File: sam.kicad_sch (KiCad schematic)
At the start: 45 parts, among them IC1 4164, IC15 MC6883, IC16 74LS244N, IC2 4164, IC3 4164, IC31 74LS02N, IC33 74LS138N, IC36 74LS132, IC37 GAL, IC4 4164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

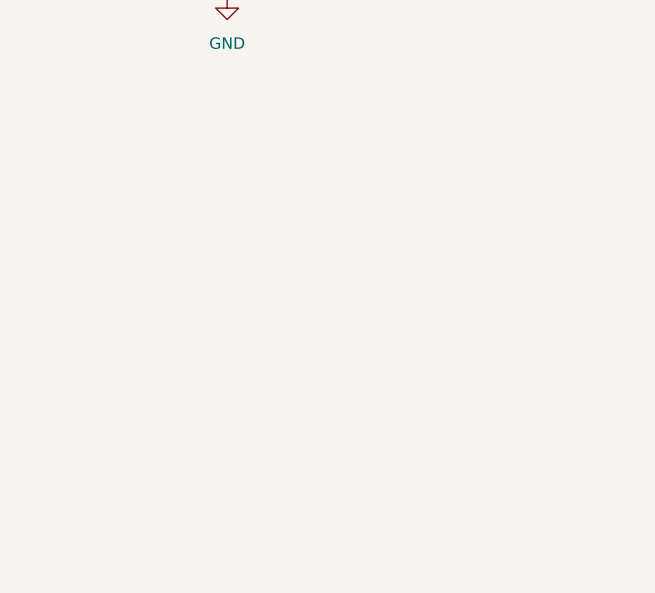
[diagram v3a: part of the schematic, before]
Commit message: add control for pia 3
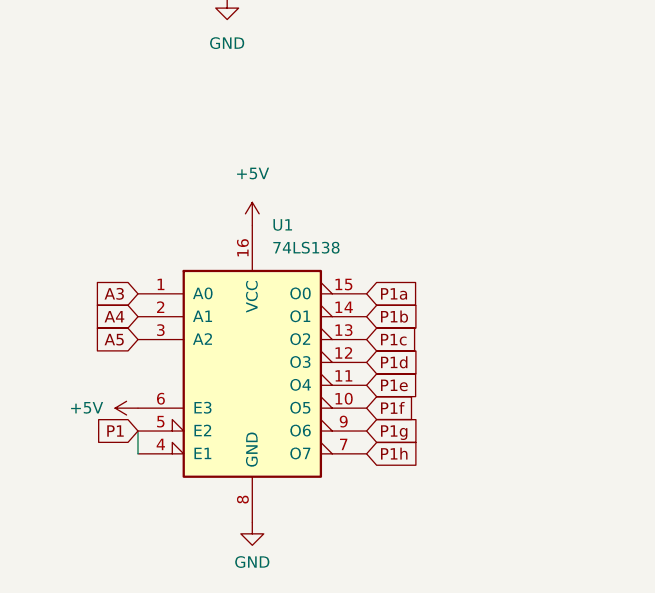
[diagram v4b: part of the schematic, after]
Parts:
- added U1: 74LS138, Package_DIP:DIP-16_W7.62mm, symbol 74xx:74LS138
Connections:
- net +5V: now also U1.16 (VCC), U1.6 (E3)
- net A3: now also U1.1 (A0)
- net A4: now also U1.2 (A1)
- net A5: now also U1.3 (A2)
- net GND: now also U1.8 (GND)
- net P1: now also U1.4 (E1), U1.5 (E2)
- new net P1a: U1.15 (O0)
- new net P1b: U1.14 (O1)
- new net P1c: U1.13 (O2)
- new net P1d: U1.12 (O3)
- new net P1e: U1.11 (O4)
- new net P1f: U1.10 (O5)
- new net P1g: U1.9 (O6)
- new net P1h: U1.7 (O7)
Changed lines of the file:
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@@
     (stroke (width 0) (type default))
   )
+  (wire (pts (xy 25.4 237.49) (xy 25.4 240.03))
+    (stroke (width 0) (type default))
+  )
   (wire (pts (xy 89.789 178.816) (xy 89.789 163.576))
     (stroke (width 0) (type default))
@@
     (stroke (width 0) (type default))
   )
+  (global_label "A5" (shape input) (at 25.4 227.33 180) (fields_autoplaced)
+    (effects (font (size 1.27 1.27)) (justify right))
+    (property "Intersheetrefs" "${INTERSHEET_REFS}" (at 20.7709 227.33 0)
+      (effects (font (size 1.27 1.27)) (justify right) hide)
+    )
+  )
   (global_label "DO0" (shape output) (at 22.606 171.45 180) (fields_autoplaced)
     (effects (font (size 1.27 1.27)) (justify right))
@@
     )
   )
+  (global_label "A3" (shape input) (at 25.4 222.25 180) (fields_autoplaced)
+    (effects (font (size 1.27 1.27)) (justify right))
+    (property "Intersheetrefs" "${INTERSHEET_REFS}" (at 20.7709 222.25 0)
+      (effects (font (size 1.27 1.27)) (justify right) hide)
+    )
+  )
   (global_label "~{WE}" (shape output) (at 110.617 112.141 180) (fields_autoplaced)
     (effects (font (size 1.27 1.27)) (justify right))
@@
     )
   )
+  (global_label "P1a" (shape input) (at 50.8 222.25 0) (fields_autoplaced)
+    (effects (font (size 1.27 1.27)) (justify left))
+    (property "Intersheetrefs" "${INTERSHEET_REFS}" (at 56.7595 222.25 0)
+      (effects (font (size 1.27 1.27)) (justify left) hide)
+    )
+  )
   (global_label "Z8" (shape output) (at 264.922 169.672 0) (fields_autoplaced)
     (effects (font (size 1.27 1.27)) (justify left))
@@
     )
   )
+  (global_label "P1d" (shape input) (at 50.8 229.87 0) (fields_autoplaced)
+    (effects (font (size 1.27 1.27)) (justify left))
+    (property "Intersheetrefs" "${INTERSHEET_REFS}" (at 56.7595 229.87 0)
+      (effects (font (size 1.27 1.27)) (justify left) hide)
+    )
+  )
   (global_label "RAM VCC" (shape passive) (at 130.937 85.471 0) (fields_autoplaced)
     (effects (font (size 1.27 1.27)) (justify left))
@@
     )
   )
+  (global_label "A4" (shape input) (at 25.4 224.79 180) (fields_autoplaced)
+    (effects (font (size 1.27 1.27)) (justify right))
+    (property "Intersheetrefs" "${INTERSHEET_REFS}" (at 20.7709 224.79 0)
+      (effects (font (size 1.27 1.27)) (justify right) hide)
+    )
+  )
   (global_label "A3" (shape output) (at 232.156 37.211 180) (fields_autoplaced)
     (effects (font (size 1.27 1.27)) (justify right))
@@
     )
   )
+  (global_label "P1h" (shape input) (at 50.8 240.03 0) (fields_autoplaced)
+    (effects (font (size 1.27 1.27)) (justify left))
+    (property "Intersheetrefs" "${INTERSHEET_REFS}" (at 56.7595 240.03 0)
+      (effects (font (size 1.27 1.27)) (justify left) hide)
+    )
+  )
   (global_label "A2" (shape output) (at 232.156 34.671 180) (fields_autoplaced)
     (effects (font (size 1.27 1.27)) (justify right))
@@
     )
   )
+  (global_label "P1f" (shape input) (at 50.8 234.95 0) (fields_autoplaced)
+    (effects (font (size 1.27 1.27)) (justify left))
+    (property "Intersheetrefs" "${INTERSHEET_REFS}" (at 56.3362 234.95 0)
+      (effects (font (size 1.27 1.27)) (justify left) hide)
+    )
+  )
   (global_label "Z1" (shape input) (at 67.945 91.694 180) (fields_autoplaced)
     (effects (font (size 1.27 1.27)) (justify right))
@@
     )
   )
+  (global_label "P1c" (shape input) (at 50.8 227.33 0) (fields_autoplaced)
+    (effects (font (size 1.27 1.27)) (justify left))
+    (property "Intersheetrefs" "${INTERSHEET_REFS}" (at 56.6991 227.33 0)
+      (effects (font (size 1.27 1.27)) (justify left) hide)
+    )
+  )
   (global_label "D2" (shape bidirectional) (at 48.006 158.75 0) (fields_autoplaced)
     (effects (font (size 1.27 1.27)) (justify left))
@@
     )
   )
+  (global_label "P1e" (shape input) (at 50.8 232.41 0) (fields_autoplaced)
+    (effects (font (size 1.27 1.27)) (justify left))
+    (property "Intersheetrefs" "${INTERSHEET_REFS}" (at 56.6991 232.41 0)
+      (effects (font (size 1.27 1.27)) (justify left) hide)
+    )
+  )
   (global_label "Z0" (shape input) (at 110.617 28.575 180) (fields_autoplaced)
     (effects (font (size 1.27 1.27)) (justify right))
@@
     )
   )
+  (global_label "P1g" (shape input) (at 50.8 237.49 0) (fields_autoplaced)
+    (effects (font (size 1.27 1.27)) (justify left))
+    (property "Intersheetrefs" "${INTERSHEET_REFS}" (at 56.7595 237.49 0)
+      (effects (font (size 1.27 1.27)) (justify left) hide)
+    )
+  )
   (global_label "A15" (shape input) (at 229.362 174.752 180) (fields_autoplaced)
     (effects (font (size 1.27 1.27)) (justify right))
@@
     )
   )
+  (global_label "P1b" (shape input) (at 50.8 224.79 0) (fields_autoplaced)
+    (effects (font (size 1.27 1.27)) (justify left))
+    (property "Intersheetrefs" "${INTERSHEET_REFS}" (at 56.7595 224.79 0)
+      (effects (font (size 1.27 1.27)) (justify left) hide)
+    )
+  )
   (global_label "S2" (shape input) (at 259.842 189.992 0) (fields_autoplaced)
     (effects (font (size 1.27 1.27)) (justify left))
@@
     )
   )
+  (global_label "P1" (shape input) (at 25.4 237.49 180) (fields_autoplaced)
+    (effects (font (size 1.27 1.27)) (justify right))
+    (property "Intersheetrefs" "${INTERSHEET_REFS}" (at 20.5963 237.4106 0)
+      (effects (font (size 1.27 1.27)) (justify right) hide)
+    )
+  )
   (global_label "~{Q}" (shape input) (at 229.362 167.132 180) (fields_autoplaced)
     (effects (font (size 1.27 1.27)) (justify right))
@@
     )
   )
+  (symbol (lib_id "74xx:74LS138") (at 38.1 229.87 0) (unit 1)
+    (in_bom yes) (on_board yes) (dnp no) (fields_autoplaced)
+    (property "Reference" "U1" (at 40.2941 214.63 0)
+      (effects (font (size 1.27 1.27)) (justify left))
+    )
+    (property "Value" "74LS138" (at 40.2941 217.17 0)
+      (effects (font (size 1.27 1.27)) (justify left))
+    )
+    (property "Footprint" "Package_DIP:DIP-16_W7.62mm" (at 38.1 229.87 0)
+      (effects (font (size 1.27 1.27)) hide)
+    )
+    (property "Datasheet" "http://www.ti.com/lit/gpn/sn74LS138" (at 38.1 229.87 0)
+      (effects (font (size 1.27 1.27)) hide)
+    )
+    (pin "1")
+    (pin "10")
+    (pin "11")
+    (pin "12")
+    (pin "13")
+    (pin "14")
+    (pin "15")
+    (pin "16")
+    (pin "2")
+    (pin "3")
+    (pin "4")
+    (pin "5")
+    (pin "6")
+    (pin "7")
+    (pin "8")
+    (pin "9")
+    (instances
+      (project "Dragon32"
+        (path "/0c3dceba-7c95-4b3d-b590-0eb581444beb/28dac1c2-804e-40fd-9ff5-acdb4226ab76"
+          (reference "U1") (unit 1)
+        )
+        (path "/0c3dceba-7c95-4b3d-b590-0eb581444beb/c0eaba02-6b8d-4a7f-b51d-5746c573781a"
+          (reference "IC10") (unit 1)
+        )
+      )
+    )
+  )
   (symbol (lib_id "74xx:74LS132") (at 238.252 132.588 0) (unit 2)
     (in_bom yes) (on_board yes) (dnp no) (fields_autoplaced)
@@
     )
   )
+  (symbol (lib_id "power:+5V") (at 38.1 214.63 0) (unit 1)
+    (in_bom yes) (on_board yes) (dnp no) (fields_autoplaced)
+    (property "Reference" "#PWR02" (at 38.1 218.44 0)
+      (effects (font (size 1.27 1.27)) hide)
+    )
+    (property "Value" "+5V" (at 38.1 208.915 0)
+      (effects (font (size 1.27 1.27)))
+    )
+    (property "Footprint" "" (at 38.1 214.63 0)
+      (effects (font (size 1.27 1.27)) hide)
+    )
+    (property "Datasheet" "" (at 38.1 214.63 0)
+      (effects (font (size 1.27 1.27)) hide)
+    )
+    (pin "1")
+    (instances
+      (project "Dragon32"
+        (path "/0c3dceba-7c95-4b3d-b590-0eb581444beb/28dac1c2-804e-40fd-9ff5-acdb4226ab76"
+          (reference "#PWR02") (unit 1)
+        )
+        (path "/0c3dceba-7c95-4b3d-b590-0eb581444beb/c0eaba02-6b8d-4a7f-b51d-5746c573781a"
+          (reference "#PWR02") (unit 1)
+        )
+      )
+    )
+  )
   (symbol (lib_id "Memory_RAM_Siemens:HYB4116") (at 78.105 103.124 0) (unit 1)
     (in_bom yes) (on_board yes) (dnp no)
@@
         )
       )
+    )
+  )
+  (symbol (lib_id "power:+5V") (at 25.4 234.95 90) (unit 1)
+    (in_bom yes) (on_board yes) (dnp no)
+    (property "Reference" "#PWR01" (at 29.21 234.95 0)
+      (effects (font (size 1.27 1.27)) hide)
+    )
+    (property "Value" "+5V" (at 17.78 234.95 90)
+      (effects (font (size 1.27 1.27)) (justify right))
+    )
+    (property "Footprint" "" (at 25.4 234.95 0)
+      (effects (font (size 1.27 1.27)) hide)
+    )
+    (property "Datasheet" "" (at 25.4 234.95 0)
+      (effects (font (size 1.27 1.27)) hide)
+    )
+    (pin "1")
+    (instances
+      (project "Dragon32"
+        (path "/0c3dceba-7c95-4b3d-b590-0eb581444beb/28dac1c2-804e-40fd-9ff5-acdb4226ab76"
+          (reference "#PWR01") (unit 1)
+        )
+        (path "/0c3dceba-7c95-4b3d-b590-0eb581444beb/c0eaba02-6b8d-4a7f-b51d-5746c573781a"
+          (reference "#PWR01") (unit 1)
+        )
+      )
+    )
+  )
+  (symbol (lib_id "power:GND") (at 38.1 247.65 0) (unit 1)
+    (in_bom yes) (on_board yes) (dnp no) (fields_autoplaced)
+    (property "Reference" "#PWR03" (at 38.1 254 0)
+      (effects (font (size 1.27 1.27)) hide)
+    )
+    (property "Value" "GND" (at 38.1 252.095 0)
+      (effects (font (size 1.27 1.27)))
+    )
+    (property "Footprint" "" (at 38.1 247.65 0)
+      (effects (font (size 1.27 1.27)) hide)
+    )
+    (property "Datasheet" "" (at 38.1 247.65 0)
+      (effects (font (size 1.27 1.27)) hide)
+    )
+    (pin "1")
+    (instances
+      (project "Dragon32"
+        (path "/0c3dceba-7c95-4b3d-b590-0eb581444beb/28dac1c2-804e-40fd-9ff5-acdb4226ab76"
+          (reference "#PWR03") (unit 1)
+        )
+        (path "/0c3dceba-7c95-4b3d-b590-0eb581444beb/c0eaba02-6b8d-4a7f-b51d-5746c573781a"
+          (reference "#PWR03") (unit 1)
+        )
+      )
